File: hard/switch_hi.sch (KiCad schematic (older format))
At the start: 5 parts, among them M2 IRLML6402TRPBF, M3 2N7002,215

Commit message: attribute naming update
JLCPCB_Part_Number -> LCSC
DigiKey_Part_Number -> DigiKey
Mouser_Part_Number -> Mouser
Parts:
- M2: DigiKey (none) -> IRLML6402PBFTR-ND; DigiKey_Part_Number IRLML6402PBFTR-ND -> (none); JLCPCB_Part_Number C2593 -> (none); LCSC (none) -> C2593; Mouser (none) -> 942-IRLML6402TRPBF; Mouser_Part_Number 942-IRLML6402TRPBF -> (none)
- M3: JLCPCB_Part_Number C65189 -> (none); LCSC (none) -> C65189
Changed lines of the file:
@@
 F 2 "Package_TO_SOT_SMD:SOT-23" H 7250 3850 50  0001 C CNN
 F 3 "https://www.infineon.com/dgdl/irlml6402pbf.pdf?fileId=5546d462533600a401535668d5c2263c" H 6100 3850 50  0001 C CNN
-F 4 "IRLML6402PBFTR-ND" H 7250 3850 50  0001 C CNN "DigiKey_Part_Number"
-F 5 "942-IRLML6402TRPBF" H 7250 3850 50  0001 C CNN "Mouser_Part_Number"
-F 6 "C2593" H 6400 3750 50  0001 C CNN "JLCPCB_Part_Number"
+F 4 "IRLML6402PBFTR-ND" H 7250 3850 50  0001 C CNN "DigiKey"
+F 5 "942-IRLML6402TRPBF" H 7250 3850 50  0001 C CNN "Mouser"
+F 6 "C2593" H 6400 3750 50  0001 C CNN "LCSC"
 F 7 "Infineon Technologies" H 7250 3850 50  0001 C CNN "MF"
 F 8 "IRLML6402TRPBF" H 7250 3850 50  0001 C CNN "MPN"
@@
 F 2 "Package_TO_SOT_SMD:SOT-23" H 6500 4100 50  0001 C CNN
 F 3 "https://assets.nexperia.com/documents/data-sheet/2N7002.pdf" H 5700 4100 50  0001 C CNN
-F 4 "C65189" H 6100 4000 50  0001 C CNN "JLCPCB_Part_Number"
+F 4 "C65189" H 6100 4000 50  0001 C CNN "LCSC"
 F 5 "Nexperia" H 6500 4100 50  0001 C CNN "MF"
 F 6 "2N7002,215" H 6500 4100 50  0001 C CNN "MPN"

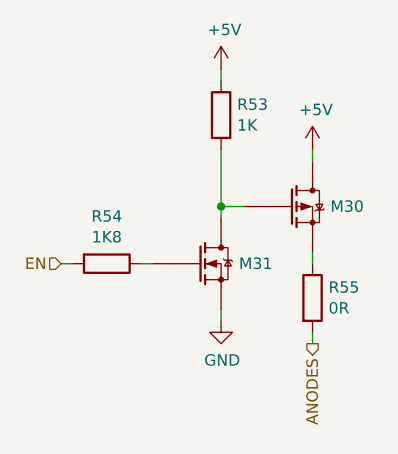
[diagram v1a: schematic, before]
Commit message: re-connect footprints
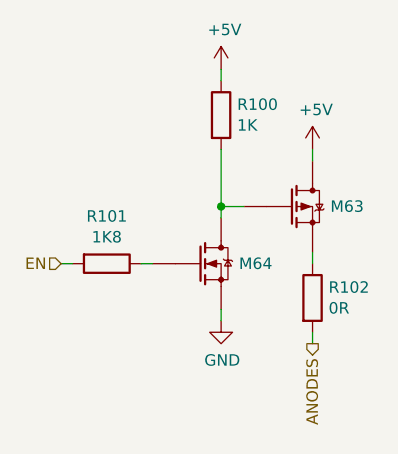
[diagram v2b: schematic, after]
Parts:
- renumbered M2 to M1, M3 to M2, R11 to R7, R12 to R8, R13 to R9
